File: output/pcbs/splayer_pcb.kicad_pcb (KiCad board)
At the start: 2 copper layers, 124.4 x 92.7 mm, 48 parts

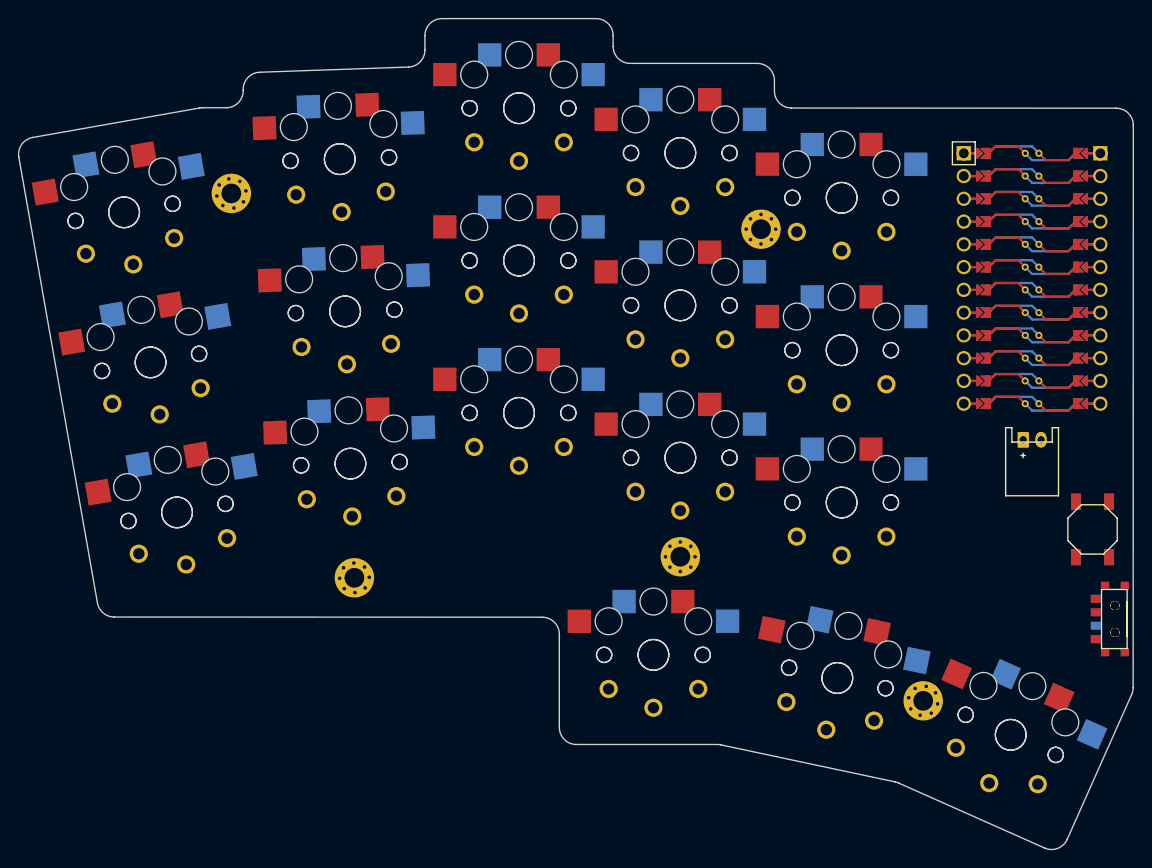
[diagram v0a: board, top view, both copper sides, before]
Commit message: updated footprints to ceoloide footprints
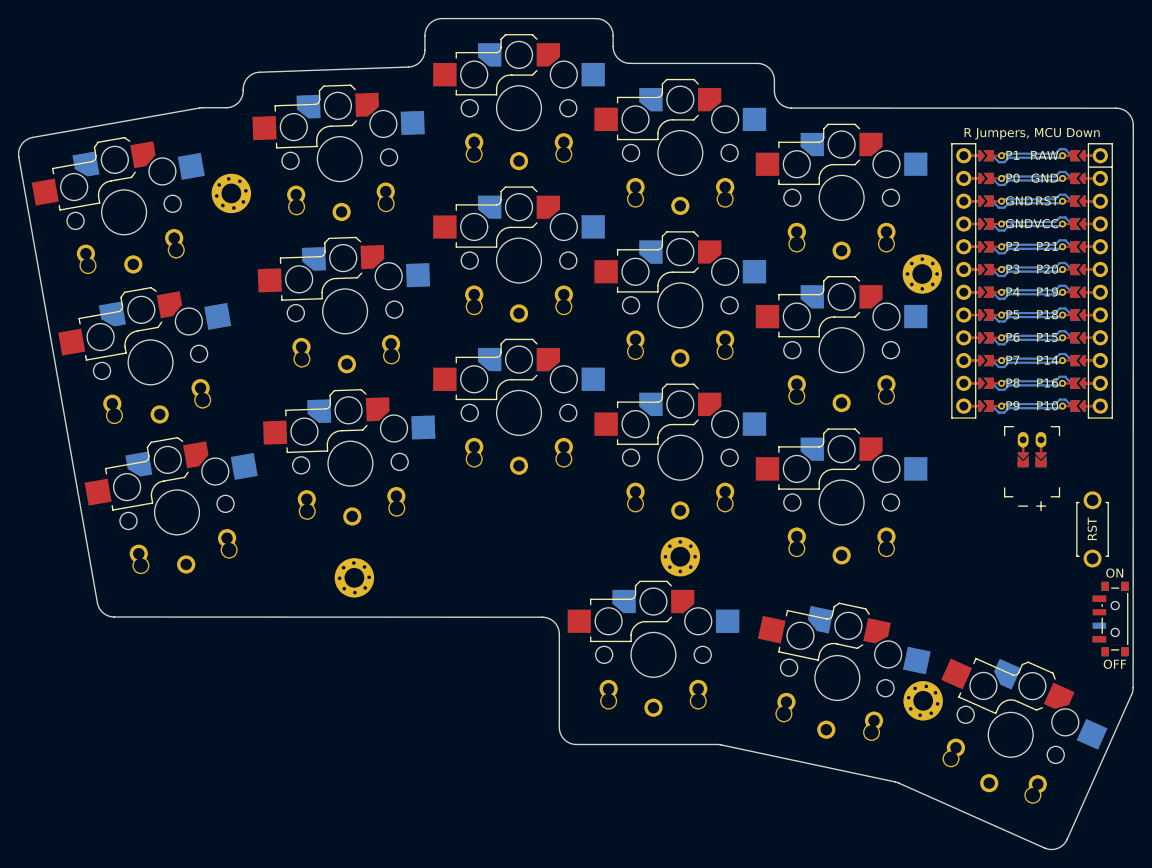
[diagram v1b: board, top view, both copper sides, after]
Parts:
- removed B1, B2: , E73:SW_TACT_ALPS_SKQGABE010
- removed JST2: , JST_PH_S2B-PH-K_02x2.00mm_Angled
- removed S19, S20, S21, S22, S23, S24, S25, S26, S27, S28, S29, S30, S31, S32, S33, S34, S35, S36: , PG1350
- removed T1, T2: , E73:SPDT_C128955
- added PWR1: , ceoloide:power_switch_smd_side, F.Cu at (204.7, 111.9)
- added RST1: , ceoloide:reset_switch_tht_top, F.Cu at (202.2, 101.9)
- JST1: footprint JST_PH_S2B-PH-K_02x2.00mm_Angled -> ceoloide:battery_connector_jst_ph_2
- MCU1: footprint ProMicro -> ceoloide:mcu_nice_nano
- S1, S10, S11, S12, S13, S14, S15, S16, S17, S18, S2, S3, S4, S5, S6, S7, S8, S9: footprint PG1350 -> ceoloide:switch_choc_v1_v2; moved to B.Cu
- moved _2 18.7 mm to (183.2, 73.4)
- moved MCU1 1.00 mm to (195.4, 72.9), turned to 0 degrees
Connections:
- JST1 pad 1: pos -> BAT_P
- MCU1 pad 1: RAW -> MCU1_1
- MCU1 pad 10: P14 -> MCU1_10
- MCU1 pad 11: P16 -> MCU1_11
- MCU1 pad 12: P10 -> MCU1_12
- MCU1 pad 13: P9 -> MCU1_13
- MCU1 pad 14: P8 -> MCU1_14
- MCU1 pad 15: P7 -> MCU1_15
- MCU1 pad 16: P6 -> MCU1_16
- MCU1 pad 17: P5 -> MCU1_17
- MCU1 pad 18: P4 -> MCU1_18
- MCU1 pad 19: P3 -> MCU1_19
- MCU1 pad 2: GND -> MCU1_2
- MCU1 pad 20: P2 -> MCU1_20
- MCU1 pad 21: GND -> MCU1_21
- MCU1 pad 22: GND -> MCU1_22
- MCU1 pad 23: P0 -> MCU1_23
- MCU1 pad 24: P1 -> MCU1_24
- MCU1 pad 3: RST -> MCU1_3
- MCU1 pad 4: VCC -> MCU1_4
- MCU1 pad 5: P21 -> MCU1_5
- MCU1 pad 6: P20 -> MCU1_6
- MCU1 pad 7: P19 -> MCU1_7
- MCU1 pad 8: P18 -> MCU1_8
- MCU1 pad 9: P15 -> MCU1_9
- S1 pad : (no net) -> GND
- S1 pad 1: P6 -> GND
- S1 pad 2: GND -> P6
- S10 pad : (no net) -> GND
- S10 pad 1: P15 -> GND
- S10 pad 2: GND -> P15
- S11 pad : (no net) -> GND
- S11 pad 1: P19 -> GND
- S11 pad 2: GND -> P19
- S12 pad : (no net) -> GND
- S12 pad 1: P21 -> GND
- S12 pad 2: GND -> P21
- S13 pad : (no net) -> GND
- S13 pad 1: P14 -> GND
- S13 pad 2: GND -> P14
- S14 pad : (no net) -> GND
- S14 pad 1: P18 -> GND
- S14 pad 2: GND -> P18
- S15 pad : (no net) -> GND
- S15 pad 1: P20 -> GND
- S15 pad 2: GND -> P20
- S16 pad : (no net) -> GND
- S16 pad 1: P9 -> GND
- S16 pad 2: GND -> P9
- S17 pad : (no net) -> GND
- S17 pad 1: P16 -> GND
- S17 pad 2: GND -> P16
- S18 pad : (no net) -> GND
- S18 pad 1: P10 -> GND
- S18 pad 2: GND -> P10
- S2 pad : (no net) -> GND
- S2 pad 1: P3 -> GND
- S2 pad 2: GND -> P3
- S3 pad : (no net) -> GND
- S3 pad 1: P1 -> GND
- S3 pad 2: GND -> P1
- S4 pad : (no net) -> GND
- S4 pad 1: P7 -> GND
- S4 pad 2: GND -> P7
- S5 pad : (no net) -> GND
- S5 pad 1: P4 -> GND
- S5 pad 2: GND -> P4
- S6 pad : (no net) -> GND
- S6 pad 1: P0 -> GND
- S6 pad 2: GND -> P0
- S7 pad : (no net) -> GND
- S7 pad 1: P8 -> GND
- S7 pad 2: GND -> P8
- S8 pad : (no net) -> GND
- S8 pad 1: P5 -> GND
- S8 pad 2: GND -> P5
- S9 pad : (no net) -> GND
- S9 pad 1: P2 -> GND
- S9 pad 2: GND -> P2
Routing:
- net (no net): track 0.00 -> 337.7 mm
- net JST1_2: track 0.00 -> 3.60 mm
- net JST1_1: track 0.00 -> 3.60 mm
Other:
- net class Default removed

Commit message: switched to ceoloide mounting hole frootprints, and designated a folder for ceoloide footprints to be consistent with the website. flushed the MCU against the inner wall of the case
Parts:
- moved RST1 16.3 mm to (185.9, 101.9)
- moved MCU1 1.49 mm to (195.4, 71.4)
- moved JST1 0.75 mm to (194.7, 91.9), turned to -90 degrees
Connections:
- MCU1 pad 10: MCU1_10 -> P7
- MCU1 pad 11: MCU1_11 -> P8
- MCU1 pad 12: MCU1_12 -> P9
- MCU1 pad 13: MCU1_13 -> P10
- MCU1 pad 14: MCU1_14 -> P16
- MCU1 pad 15: MCU1_15 -> P14
- MCU1 pad 16: MCU1_16 -> P15
- MCU1 pad 17: MCU1_17 -> P18
- MCU1 pad 18: MCU1_18 -> P19
- MCU1 pad 19: MCU1_19 -> P20
- MCU1 pad 20: MCU1_20 -> P21
- MCU1 pad 5: MCU1_5 -> P2
- MCU1 pad 6: MCU1_6 -> P3
- MCU1 pad 7: MCU1_7 -> P4
- MCU1 pad 8: MCU1_8 -> P5
- MCU1 pad 9: MCU1_9 -> P6
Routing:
- net (no net): track 337.7 -> 112.6 mm

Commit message: redefined mounting holes positions
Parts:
- removed _1, _2, _3, _4, _5: , MountingHole_2.2mm_M2_Pad_Via
- added MH1: , ceoloide:mounting_hole_npth, F.Cu at (203.5, 114.6)
- added MH2: , ceoloide:mounting_hole_npth, F.Cu at (187.1, 107.3)
- added MH3: , ceoloide:mounting_hole_npth, F.Cu at (106.1, 64.4)
- added MH4: , ceoloide:mounting_hole_npth, F.Cu at (165.2, 68.4)
- added MH5: , ceoloide:mounting_hole_npth, F.Cu at (108.3, 83.0)
- added MH6: , ceoloide:mounting_hole_npth, F.Cu at (138.2, 107.6)
- added MH7: , ceoloide:mounting_hole_npth, F.Cu at (183.4, 122.4)
- RST1: footprint ceoloide:reset_switch_tht_top -> ceoloide:reset_button_smd_side
- moved RST1 19.5 mm to (204.7, 96.9), turned to -90 degrees
- moved PWR1 5.00 mm to (204.7, 106.9)
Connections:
- RST1 pad 1: RST -> GND
- RST1 pad 2: GND -> RST
- S1 pad 2: P6 -> GND
- S10 pad 2: P15 -> GND
- S11 pad 2: P19 -> GND
- S12 pad 2: P21 -> GND
- S13 pad 2: P14 -> GND
- S14 pad 2: P18 -> GND
- S15 pad 2: P20 -> GND
- S16 pad 2: P9 -> GND
- S17 pad 2: P16 -> GND
- S18 pad 2: P10 -> GND
- S2 pad 2: P3 -> GND
- S3 pad 2: P1 -> GND
- S4 pad 2: P7 -> GND
- S5 pad 2: P4 -> GND
- S6 pad 2: P0 -> GND
- S7 pad 2: P8 -> GND
- S8 pad 2: P5 -> GND
- S9 pad 2: P2 -> GND
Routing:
- net (no net): track 112.6 -> 0.00 mm
- net GND: track 0.00 -> 29.5 mm
- net RAW: track 0.00 -> 9.84 mm
- net VCC: track 0.00 -> 9.84 mm
- net RST: track 0.00 -> 9.84 mm
- net P1: track 0.00 -> 9.83 mm
- net P0: track 0.00 -> 9.83 mm
- net MCU1_4: track 0.00 -> 4.24 mm
- net MCU1_3: track 0.00 -> 4.24 mm
- net MCU1_24: track 0.00 -> 4.24 mm
- net MCU1_23: track 0.00 -> 4.24 mm
- net MCU1_22: track 0.00 -> 4.24 mm
- net MCU1_21: track 0.00 -> 4.24 mm
- net MCU1_2: track 0.00 -> 4.24 mm
- net MCU1_1: track 0.00 -> 4.24 mm
